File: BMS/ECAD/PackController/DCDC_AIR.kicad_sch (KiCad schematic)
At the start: 33 parts, among them K1901 KT12-1A-40L-THT, Q1901 IXTA08N100D2HV, Q1902 IRLML0100TR, Q1903 BC846, Q1904 DMP4065S-7, U1901 TCLT1004, U1902 TCLT1004, U1903 TEA1-0505HI

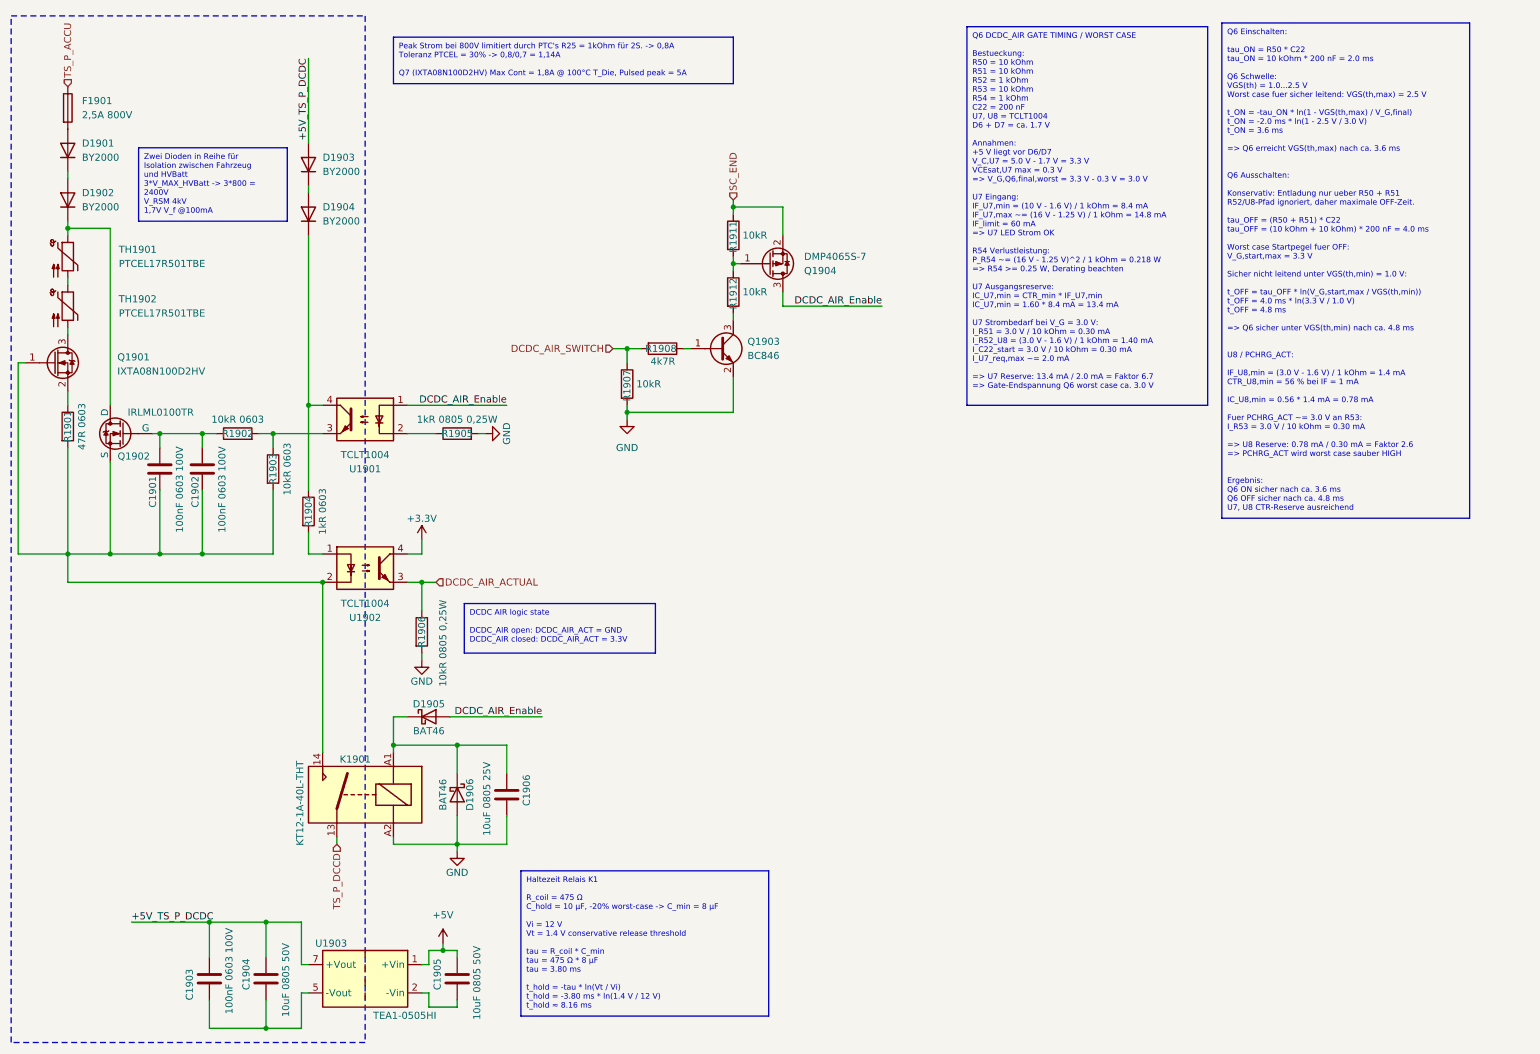
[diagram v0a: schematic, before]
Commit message: finalised schematic of pack controller
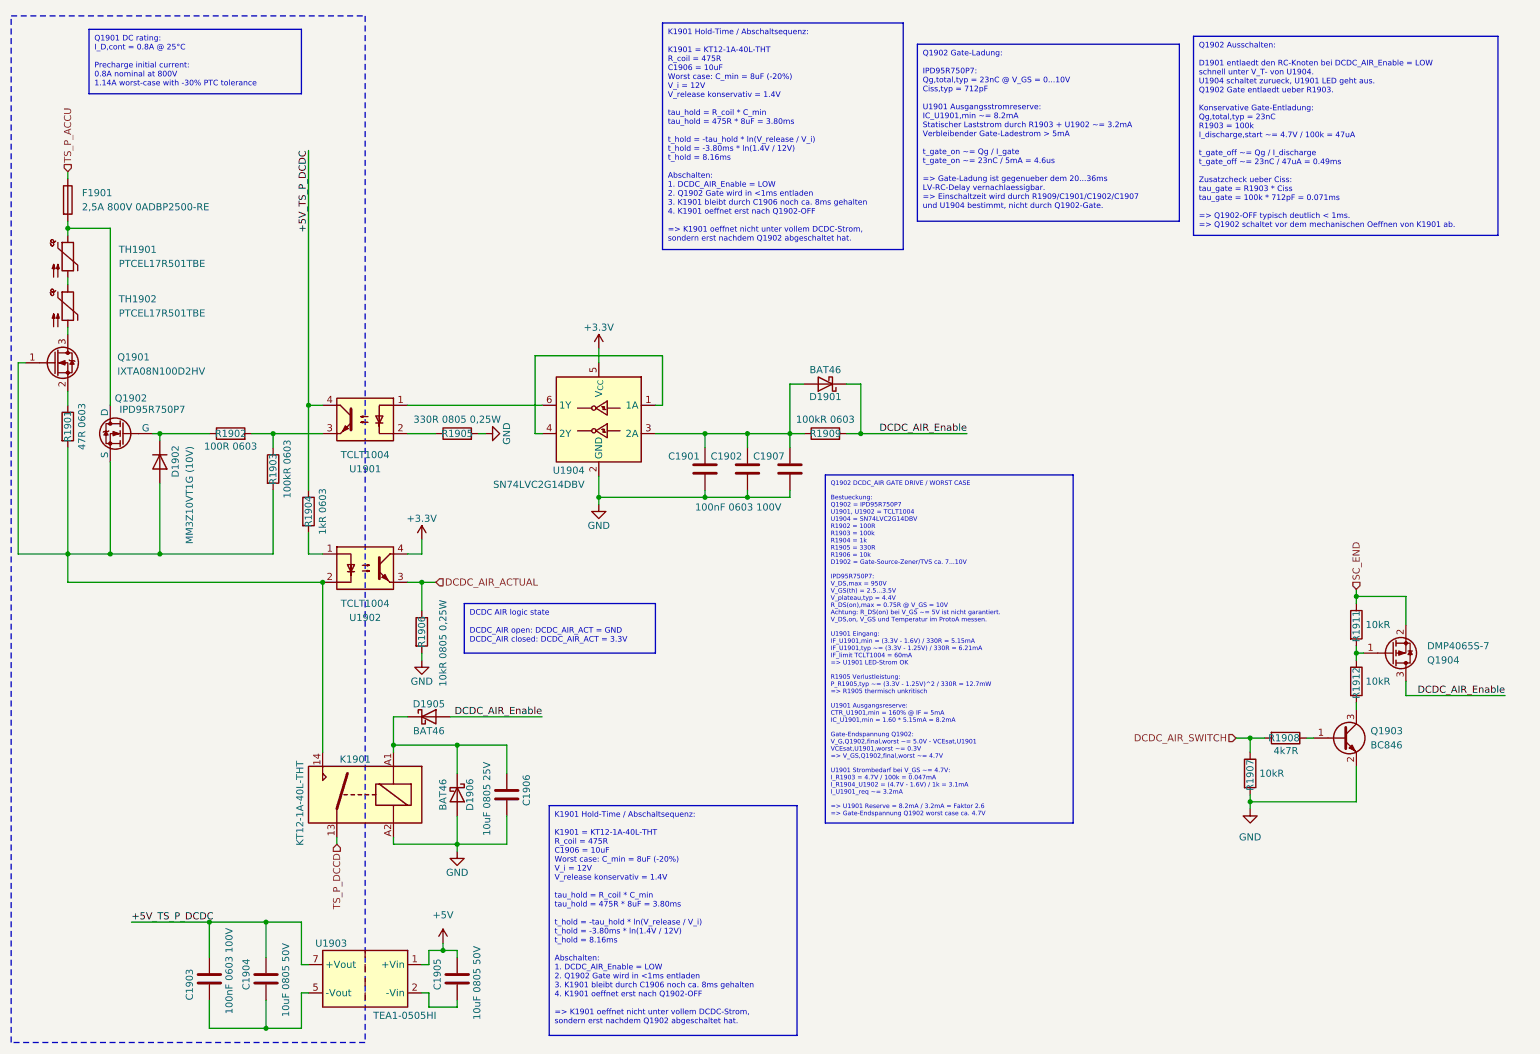
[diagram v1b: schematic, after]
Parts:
- removed D1901, D1903, D1904: BY2000, Diode_THT:D_DO-201AE_P12.70mm_Horizontal, symbol Device:D
- added C1907: 100nF 0603 100V, Capacitor_SMD:C_0603_1608Metric_Pad1.08x0.95mm_HandSolder, symbol Device:C
- added D1901: BAT46, Diode_SMD:D_SOD-123, symbol Diode:BAT46
- added R1909: 100kR 0603, Resistor_SMD:R_0603_1608Metric_Pad0.98x0.95mm_HandSolder, symbol Device:R
- added U1904: SN74LVC2G14DBV, Package_TO_SOT_SMD:SOT-23-6, symbol 74xGxx:SN74LVC2G14DBV
- D1902: value BY2000 -> MM3Z10VT1G (10V); footprint Diode_THT:D_DO-201AE_P12.70mm_Horizontal -> Diode_SMD:D_SOD-323_HandSoldering; PartNr. (none) -> MM3Z3V3T1G
- F1901: value 2,5A 800V -> 2,5A 800V 0ADBP2500-RE; footprint (none) -> Resistor_THT:R_Axial_Power_L38.0mm_W6.4mm_P40.64mm
- K1901: footprint (none) -> EKartParts:Meder_KT_Relay
- Q1902: value IRLML0100TR -> IPD95R750P7; footprint Package_TO_SOT_SMD:SOT-23-3 -> Package_TO_SOT_SMD:TO-252-2
- R1902: value 10kR 0603 -> 100R 0603
- R1903: value 10kR 0603 -> 100kR 0603
- R1905: value 1kR 0805 0,25W -> 330R 0805 0,25W
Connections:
- net +3.3V: now also U1904.5 (V_{CC})
- net +5V_TS_P_DCDC: now also R1904.1, U1901.4
- net DCDC_AIR_Enable: now also D1901.1 (K), R1909.2; no longer U1901.1
- net GND: now also C1901.1, C1902.1, C1907.1, U1904.2 (GND)
- net at K1901.14, Q1901.1 (G), Q1902.3 (S)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: now also D1902.2 (A); no longer C1901.1, C1902.1
- net at Q1902.1 (D), TH1901.1: now also F1901.2; no longer D1902.1 (K)
- net at C1901.2, C1902.2: now also C1907.2, D1901.2 (A), R1909.1, U1904.3 (2A); no longer Q1902.2 (G), R1902.1
- new net: D1902.1 (K), Q1902.2 (G), R1902.1
- new net: U1904.1 (1A), U1904.4 (2Y)
- new net: U1901.1, U1904.6 (1Y)
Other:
- moved on the sheet: F1901, Q1903, Q1904, R1902, R1907, R1908, R1911, R1912

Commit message: many fixes
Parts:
- added R1910: 500R 0805, Resistor_SMD:R_0805_2012Metric_Pad1.20x1.40mm_HandSolder, symbol Device:R
- R1901: footprint Resistor_SMD:R_0603_1608Metric_Pad0.98x0.95mm_HandSolder -> Resistor_SMD:R_1206_3216Metric
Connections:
- net +5V_TS_P_DCDC: now also R1910.2
- net TS_P_DCDC: now reaches C1903.1, C1904.2, U1903.5 (-Vout)
- net TS_P_DCDC: now also R1910.1
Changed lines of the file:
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@@
+	)
+	(junction
+		(at 49.53 194.31)
+		(diameter 0)
+		(color 0 0 0 0)
 	)
 	(junction
@@
 	)
 	(junction
+		(at 43.18 194.31)
+		(diameter 0)
+		(color 0 0 0 0)
+	)
+	(junction
 		(at 138.43 99.06)
+		(diameter 0)
+		(color 0 0 0 0)
+	)
+	(junction
+		(at 43.18 175.26)
 		(diameter 0)
 		(color 0 0 0 0)
@@
 	(wire
 		(pts
+			(xy 43.18 194.31) (xy 49.53 194.31)
+		)
+		(stroke
+			(width 0)
+			(type default)
+		)
+	)
+	(wire
+		(pts
 			(xy 93.98 181.61) (xy 93.98 180.34)
 		)
@@
 	(wire
 		(pts
+			(xy 49.53 194.31) (xy 59.69 194.31)
+		)
+		(stroke
+			(width 0)
+			(type default)
+		)
+	)
+	(wire
+		(pts
 			(xy 93.98 148.59) (xy 93.98 143.51)
 		)
@@
 	(wire
 		(pts
-			(xy 35.56 175.26) (xy 49.53 175.26)
+			(xy 43.18 175.26) (xy 43.18 181.61)
+		)
+		(stroke
+			(width 0)
+			(type default)
+		)
+	)
+	(wire
+		(pts
+			(xy 35.56 175.26) (xy 43.18 175.26)
 		)
 		(stroke
@@
 	(wire
 		(pts
-			(xy 49.53 189.23) (xy 49.53 194.31)
-		)
-		(stroke
-			(width 0)
-			(type default)
-		)
-	)
-	(wire
-		(pts
 			(xy 85.09 114.3) (xy 87.63 114.3)
 		)
@@
 	(wire
 		(pts
-			(xy 49.53 194.31) (xy 59.69 194.31)
+			(xy 41.91 194.31) (xy 43.18 194.31)
 		)
 		(stroke
@@
 	(wire
 		(pts
+			(xy 43.18 175.26) (xy 49.53 175.26)
+		)
+		(stroke
+			(width 0)
+			(type default)
+		)
+	)
+	(wire
+		(pts
 			(xy 129.54 87.63) (xy 138.43 87.63)
+		)
+		(stroke
+			(width 0)
+			(type default)
+		)
+	)
+	(wire
+		(pts
+			(xy 49.53 194.31) (xy 49.53 189.23)
+		)
+		(stroke
+			(width 0)
+			(type default)
+		)
+	)
+	(wire
+		(pts
+			(xy 43.18 189.23) (xy 43.18 194.31)
 		)
 		(stroke
@@
 		(shape input)
 		(at 72.39 161.29 270)
+		(effects
+			(font
+				(size 1.27 1.27)
+			)
+			(justify right)
+		)
+	)
+	(hierarchical_label "TS_P_DCDC"
+		(shape input)
+		(at 41.91 194.31 180)
 		(effects
 			(font
@@
 			)
 		)
-		(property "Footprint" "Resistor_SMD:R_0603_1608Metric_Pad0.98x0.95mm_HandSolder"
+		(property "Footprint" "Resistor_SMD:R_1206_3216Metric"
 			(at 22.352 86.36 90)
 			(hide yes)
@@
 					(unit 1)
 				)
+			)
+		)
+	)
+	(symbol
+		(lib_id "Device:R")
+		(at 43.18 185.42 180)
+		(unit 1)
+		(body_style 1)
+		(exclude_from_sim no)
+		(in_bom yes)
+		(on_board yes)
+		(in_pos_files yes)
+		(dnp no)
+		(property "Reference" "R1910"
+			(at 43.18 185.42 90)
+			(show_name no)
+			(do_not_autoplace no)
+			(effects
+				(font
+					(size 1.27 1.27)
+				)
+			)
+		)
+		(property "Value" "500R 0805"
+			(at 40.64 185.42 90)
+			(show_name no)
+			(do_not_autoplace no)
+			(effects
+				(font
+					(size 1.27 1.27)
+				)
+			)
+		)
+		(property "Footprint" "Resistor_SMD:R_0805_2012Metric_Pad1.20x1.40mm_HandSolder"
+			(at 44.958 185.42 90)
+			(hide yes)
+			(show_name no)
+			(do_not_autoplace no)
+			(effects
+				(font
+					(size 1.27 1.27)
+				)
+			)
+		)
+		(property "Datasheet" ""
+			(at 43.18 185.42 0)
+			(hide yes)
+			(show_name no)
+			(do_not_autoplace no)
+			(effects
+				(font
+					(size 1.27 1.27)
+				)
+			)
+		)
+		(property "Description" ""
+			(at 43.18 185.42 0)
+			(show_name no)
+			(do_not_autoplace no)
+			(effects
+				(font
+					(size 1.27 1.27)
+				)
+			)
+		)
+		(pin "1"
+		)
+		(pin "2"
+		)
+		(instances
+			(project "Pack_Controller"
+				(path "/58a1c93e-baba-4d23-9191-955e00968735/b3a91e7b-f813-4b7e-8a66-9207449a05f0"
+					(reference "R1910")
+					(unit 1)
+				)

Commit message: add rule areas for hv separation
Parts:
- R1910: value 500R 0805 -> 270R 0805; now not fitted
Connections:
- net TS_P_DCCD is gone; now on net TS_P_DCDC: K1901.13
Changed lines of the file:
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@@
 		)
 	)
-	(hierarchical_label "TS_P_DCCD"
+	(hierarchical_label "TS_P_DCDC"
 		(shape input)
 		(at 72.39 161.29 270)
@@
 		)
 	)
+	(netclass_flag ""
+		(length 2.54)
+		(shape round)
+		(at 59.69 175.26 0)
+		(fields_autoplaced yes)
+		(effects
+			(font
+				(size 1.27 1.27)
+			)
+			(justify left bottom)
+		)
+		(property "Netzklasse" "HV800"
+			(at 60.3885 172.72 0)
+			(show_name no)
+			(do_not_autoplace no)
+			(effects
+				(font
+					(size 1.27 1.27)
+				)
+				(justify left)
+			)
+		)
+		(property "Component Class" ""
+			(at 36.83 96.52 0)
+			(show_name no)
+			(do_not_autoplace no)
+			(effects
+				(font
+					(size 1.27 1.27)
+					(italic yes)
+				)
+			)
+		)
+	)
+	(netclass_flag ""
+		(length 2.54)
+		(shape round)
+		(at 49.53 109.22 0)
+		(fields_autoplaced yes)
+		(effects
+			(font
+				(size 1.27 1.27)
+			)
+			(justify left bottom)
+		)
+		(property "Netzklasse" "HV800"
+			(at 50.2285 106.68 0)
+			(show_name no)
+			(do_not_autoplace no)
+			(effects
+				(font
+					(size 1.27 1.27)
+				)
+				(justify left)
+			)
+		)
+		(property "Component Class" ""
+			(at 26.67 30.48 0)
+			(show_name no)
+			(do_not_autoplace no)
+			(effects
+				(font
+					(size 1.27 1.27)
+					(italic yes)
+				)
+			)
+		)
+	)
+	(netclass_flag ""
+		(length 2.54)
+		(shape round)
+		(at 67.31 64.77 90)
+		(fields_autoplaced yes)
+		(effects
+			(font
+				(size 1.27 1.27)
+			)
+			(justify left bottom)
+		)
+		(property "Netzklasse" "HV800"
+			(at 64.77 64.0715 90)
+			(show_name no)
+			(do_not_autoplace no)
+			(effects
+				(font
+					(size 1.27 1.27)
+				)
+				(justify left)
+			)
+		)
+		(property "Component Class" ""
+			(at 44.45 -13.97 0)
+			(show_name no)
+			(do_not_autoplace no)
+			(effects
+				(font
+					(size 1.27 1.27)
+					(italic yes)
+				)
+			)
+		)
+	)
+	(netclass_flag ""
+		(length 2.54)
+		(shape round)
+		(at 31.75 50.8 0)
+		(fields_autoplaced yes)
+		(effects
+			(font
+				(size 1.27 1.27)
+			)
+			(justify left bottom)
+		)
+		(property "Netzklasse" "HV800"
+			(at 32.4485 48.26 0)
+			(show_name no)
+			(do_not_autoplace no)
+			(effects
+				(font
+					(size 1.27 1.27)
+				)
+				(justify left)
+			)
+		)
+		(property "Component Class" ""
+			(at 8.89 -27.94 0)
+			(show_name no)
+			(do_not_autoplace no)
+			(effects
+				(font
+					(size 1.27 1.27)
+					(italic yes)
+				)
+			)
+		)
+	)
 	(symbol
 		(lib_id "power:GND")
@@
 		(on_board yes)
 		(in_pos_files yes)
-		(dnp no)
+		(dnp yes)
 		(property "Reference" "R1910"
 			(at 43.18 185.42 90)
@@
 			)
 		)
-		(property "Value" "500R 0805"
+		(property "Value" "270R 0805"
 			(at 40.64 185.42 90)
 			(show_name no)

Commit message: route HV components
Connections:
- net GND: now also C1905.2, U1903.2 (-Vin)
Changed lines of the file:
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@@
 		(company "Lukas Elektronik")
-	)
-	(rectangle
-		(start 13.97 12.7)
-		(end 77.47 196.85)
-		(stroke
-			(width 0)
-			(type dash)
-			(color 255 0 0 1)
-		)
-		(fill
-			(type none)
-		)
 	)
 	(text_box "Q1902 Gate-Ladung:\n\nIPD95R750P7:\nQg,total,typ = 23nC @ V_GS = 0...10V\nCiss,typ = 712pF\n\nU1901 Ausgangsstromreserve:\nIC_U1901,min ~= 8.2mA\nStatischer Laststrom durch R1903 + U1902 ~= 3.2mA\nVerbleibender Gate-Ladestrom > 5mA\n\nt_gate_on ~= Qg / I_gate\nt_gate_on ~= 23nC / 5mA = 4.6us\n\n=> Gate-Ladung ist gegenueber dem 20...36ms\n   LV-RC-Delay vernachlaessigbar.\n=> Einschaltzeit wird durch R1909/C1901/C1902/C1907\n   und U1904 bestimmt, nicht durch Q1902-Gate."
@@
 	)
 	(junction
+		(at 91.44 190.5)
+		(diameter 0)
+		(color 0 0 0 0)
+	)
+	(junction
 		(at 91.44 180.34)
 		(diameter 0)
@@
 	(wire
 		(pts
-			(xy 93.98 190.5) (xy 88.9 190.5)
+			(xy 93.98 190.5) (xy 91.44 190.5)
 		)
 		(stroke
@@
 		(pts
 			(xy 66.04 187.96) (xy 66.04 194.31)
+		)
+		(stroke
+			(width 0)
+			(type default)
+		)
+	)
+	(wire
+		(pts
+			(xy 91.44 190.5) (xy 88.9 190.5)
 		)
 		(stroke
@@
 		)
 	)
+	(rule_area
+		(exclude_from_sim no)
+		(in_bom yes)
+		(on_board yes)
+		(dnp no)
+		(polyline
+			(pts
+				(xy 76.2 48.26) (xy 30.48 48.26) (xy 27.94 48.26) (xy 27.94 151.13) (xy 76.835 151.13) (xy 76.2 62.23)
+				(xy 76.2 59.69) (xy 76.2 57.15)
+			)
+			(stroke
+				(width 0)
+				(type dash)
+				(color 255 255 0 1)
+			)
+			(fill
+				(type reverse_hatch)
+				(color 255 255 0 0.2)
+			)
+		)
+	)
+	(rule_area
+		(exclude_from_sim no)
+		(in_bom yes)
+		(on_board yes)
+		(dnp no)
+		(polyline
+			(pts
+				(xy 76.835 152.4) (xy 30.48 152.4) (xy 27.94 152.4) (xy 27.94 195.58) (xy 76.835 195.58) (xy 76.835 166.37)
+				(xy 76.835 163.83) (xy 76.835 161.29)
+			)
+			(stroke
+				(width 0)
+				(type dash)
+				(color 194 0 194 1)
+			)
+			(fill
+				(type reverse_hatch)
+				(color 194 0 194 0.1882352941)
+			)
+		)
+	)
+	(rule_area
+		(exclude_from_sim no)
+		(in_bom yes)
+		(on_board yes)
+		(dnp no)
+		(polyline
+			(pts
+				(xy 13.97 12.7) (xy 76.835 12.7) (xy 77.47 196.85) (xy 13.97 196.85)
+			)
+			(stroke
+				(width 0)
+				(type dash)
+				(color 255 153 0 1)
+			)
+			(fill
+				(type hatch)
+				(color 255 153 0 0.2)
+			)
+		)
+	)
 	(netclass_flag ""
 		(length 2.54)
 		(shape round)
-		(at 59.69 175.26 0)
-		(fields_autoplaced yes)
+		(at 44.45 48.26 180)
 		(effects
 			(font
 				(size 1.27 1.27)
 			)
-			(justify left bottom)
-		)
-		(property "Netzklasse" "HV800"
-			(at 60.3885 172.72 0)
+			(justify right bottom)
+		)
+		(property "Netzklasse" "LOCAL_P_DCDC"
+			(at 45.1485 50.8 0)
 			(show_name no)
 			(do_not_autoplace no)
@@
 		)
 		(property "Component Class" ""
-			(at 36.83 96.52 0)
+			(at 21.59 -30.48 0)
 			(show_name no)
 			(do_not_autoplace no)
@@
 		(length 2.54)
 		(shape round)
-		(at 49.53 109.22 0)
-		(fields_autoplaced yes)
+		(at 30.48 152.4 180)
 		(effects
 			(font
 				(size 1.27 1.27)
 			)
-			(justify left bottom)
-		)
-		(property "Netzklasse" "HV800"
-			(at 50.2285 106.68 0)
+			(justify right bottom)
+		)
+		(property "Netzklasse" "P_DCDC_+5"
+			(at 31.1785 154.94 0)
 			(show_name no)
 			(do_not_autoplace no)
@@
 		)
 		(property "Component Class" ""
-			(at 26.67 30.48 0)
+			(at 7.62 73.66 0)
 			(show_name no)
 			(do_not_autoplace no)
@@
 		(length 2.54)
 		(shape round)
-		(at 31.75 50.8 0)
+		(at 17.78 12.7 180)
 		(fields_autoplaced yes)
 		(effects
@@
 				(size 1.27 1.27)
 			)
-			(justify left bottom)
+			(justify right bottom)
 		)
 		(property "Netzklasse" "HV800"
-			(at 32.4485 48.26 0)
+			(at 18.4785 15.24 0)
 			(show_name no)
 			(do_not_autoplace no)
@@
 		)
 		(property "Component Class" ""
-			(at 8.89 -27.94 0)
+			(at -5.08 -66.04 0)
 			(show_name no)
 			(do_not_autoplace no)
@@
 					(unit 1)
 				)
+			)
+		)
+	)
+	(symbol
+		(lib_id "power:GND")
+		(at 91.44 190.5 0)
+		(unit 1)
+		(body_style 1)
+		(exclude_from_sim no)
+		(in_bom yes)
+		(on_board yes)
+		(in_pos_files yes)
+		(dnp no)
+		(property "Reference" "#PWR01909"
+			(at 91.44 196.85 0)
+			(hide yes)
+			(show_name no)
+			(do_not_autoplace no)
+			(effects
+				(font
+					(size 1.27 1.27)
+				)
+			)
+		)
+		(property "Value" "GND"
+			(at 91.44 194.31 0)
+			(show_name no)
+			(do_not_autoplace no)
+			(effects
+				(font
+					(size 1.27 1.27)
+				)
+			)
+		)
+		(property "Footprint" ""
+			(at 91.44 190.5 0)
+			(hide yes)
+			(show_name no)
+			(do_not_autoplace no)
+			(effects
+				(font
+					(size 1.27 1.27)
+				)
+			)
+		)
+		(property "Datasheet" ""
+			(at 91.44 190.5 0)
+			(hide yes)
+			(show_name no)
+			(do_not_autoplace no)
+			(effects
+				(font
+					(size 1.27 1.27)
+				)
+			)
+		)
+		(property "Description" ""
+			(at 91.44 190.5 0)
+			(show_name no)
+			(do_not_autoplace no)
+			(effects
+				(font
+					(size 1.27 1.27)
+				)
+			)
+		)
+		(pin "1"
+		)
+		(instances
+			(project "Pack_Controller"
+				(path "/58a1c93e-baba-4d23-9191-955e00968735/b3a91e7b-f813-4b7e-8a66-9207449a05f0"
+					(reference "#PWR01909")
+					(unit 1)
+				)
